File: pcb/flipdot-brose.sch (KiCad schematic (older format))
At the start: 5 parts, among them J1 Conn_02x30_Odd_Even, J2 Conn_01x03, U1 ESP32_DEVCITV1

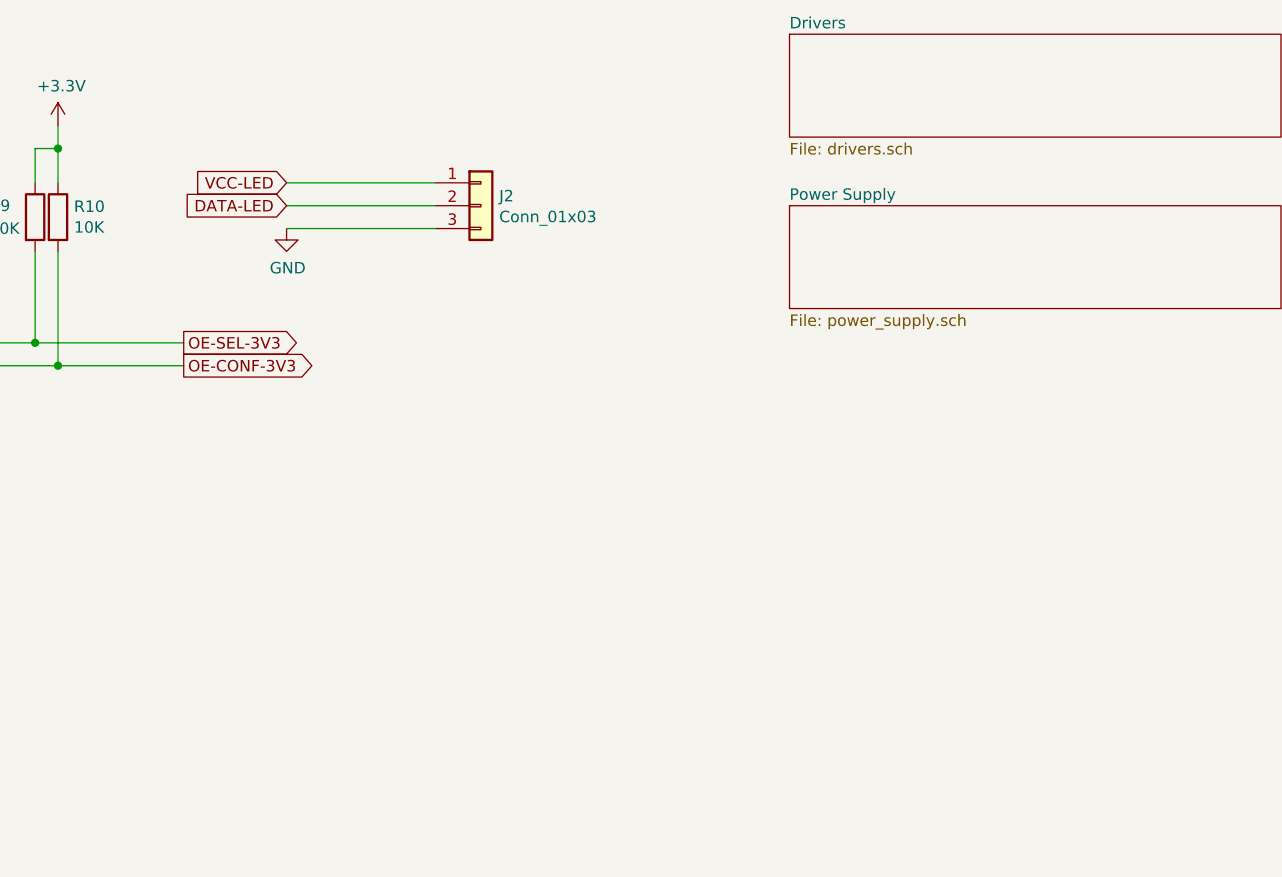
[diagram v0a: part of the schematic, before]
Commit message: resistor/capacitor for leds
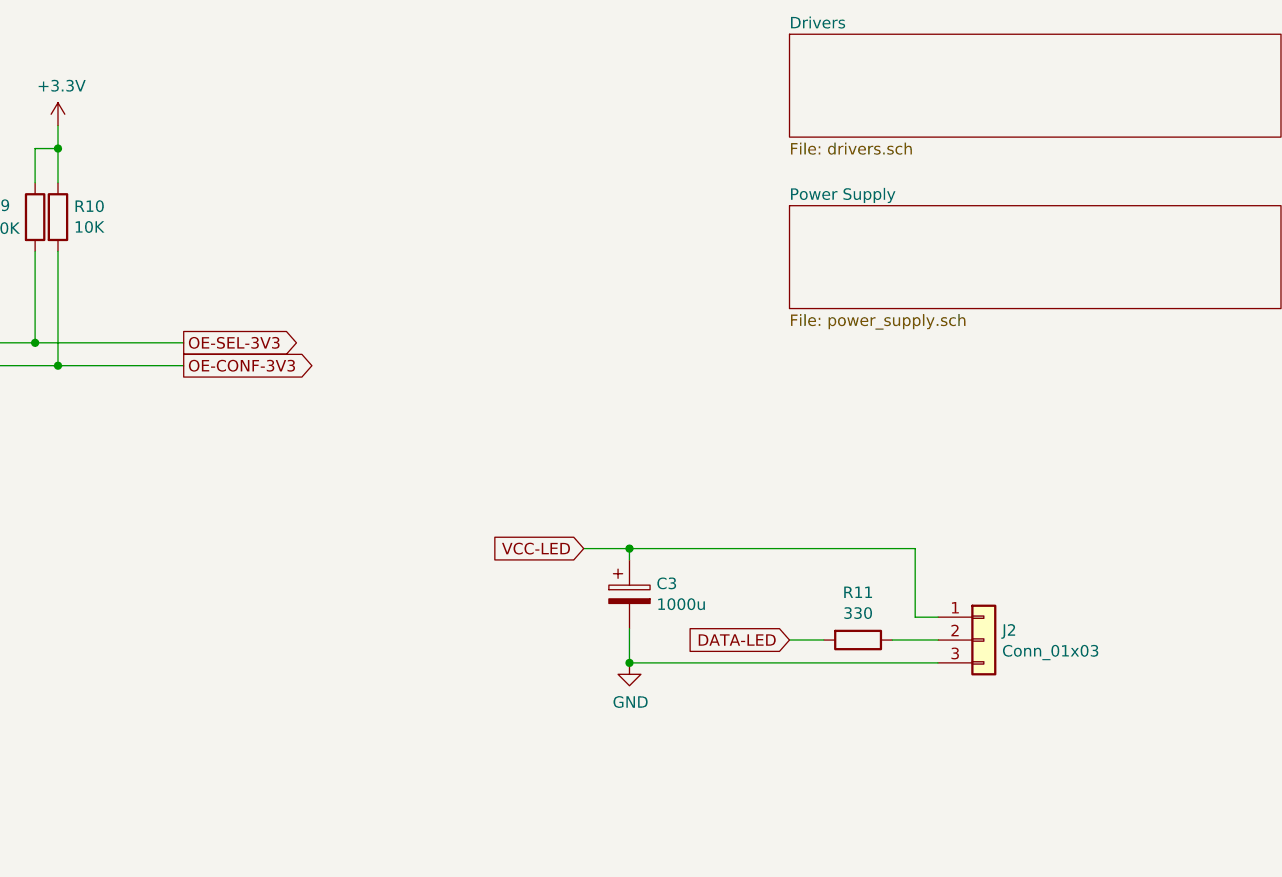
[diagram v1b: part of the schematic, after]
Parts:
- added C3: 1000u, Capacitor_THT:CP_Radial_D10.0mm_P5.00mm, symbol Device:CP
- added R11: 330, Resistor_THT:R_Axial_DIN0204_L3.6mm_D1.6mm_P5.08mm_Horizontal, symbol Device:R
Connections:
- net DATA-LED: now also R11.2; no longer J2.2 (Pin_2)
- net GND: now also C3.2
- net VCC-LED: now also C3.1
- new net: J2.2 (Pin_2), R11.1
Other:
- moved on the sheet: J2
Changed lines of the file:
@@
 	4400 2600 4600 2600
 Wire Wire Line
-	7250 1500 6600 1500
-Wire Wire Line
-	7250 1600 6600 1600
+	9450 3400 9250 3400
 $Comp
 L power:GND #PWR0102
 U 1 1 5DDF6886
-P 6600 1600
-F 0 "#PWR0102" H 6600 1350 50  0001 C CNN
-F 1 "GND" H 6605 1427 50  0000 C CNN
-F 2 "" H 6600 1600 50  0001 C CNN
-F 3 "" H 6600 1600 50  0001 C CNN
-	1    6600 1600
-	1    0    0    -1
-$EndComp
-Text GLabel 6600 1400 0    50   Input ~ 0
+P 8100 3500
+F 0 "#PWR0102" H 8100 3250 50  0001 C CNN
+F 1 "GND" H 8105 3327 50  0000 C CNN
+F 2 "" H 8100 3500 50  0001 C CNN
+F 3 "" H 8100 3500 50  0001 C CNN
+	1    8100 3500
+	1    0    0    -1
+$EndComp
+Text GLabel 7900 3000 0    50   Input ~ 0
 VCC-LED
-Text GLabel 6600 1500 0    50   Input ~ 0
+Text GLabel 8800 3400 0    50   Input ~ 0
 DATA-LED
 Wire Wire Line
@@
 L Connector_Generic:Conn_01x03 J2
 U 1 1 5DEADF32
-P 7450 1500
-F 0 "J2" H 7530 1542 50  0000 L CNN
-F 1 "Conn_01x03" H 7530 1451 50  0000 L CNN
-F 2 "Connectors_JST:JST_VH_B3PS-VH_2x3x3.96mm_Horizontal" H 7450 1500 50  0001 C CNN
-F 3 "~" H 7450 1500 50  0001 C CNN
-	1    7450 1500
-	1    0    0    -1
-$EndComp
-Wire Wire Line
-	6600 1400 7250 1400
+P 9650 3400
+F 0 "J2" H 9730 3442 50  0000 L CNN
+F 1 "Conn_01x03" H 9730 3351 50  0000 L CNN
+F 2 "Connectors_JST:JST_VH_B3PS-VH_2x3x3.96mm_Horizontal" H 9650 3400 50  0001 C CNN
+F 3 "~" H 9650 3400 50  0001 C CNN
+	1    9650 3400
+	1    0    0    -1
+$EndComp
 Wire Wire Line
 	5500 2100 6150 2100
@@
 	4400 1700 4600 1700
 NoConn ~ 4400 2100
+$Comp
+L Device:R R11
+U 1 1 5E7E658D
+P 9100 3400
+F 0 "R11" V 8893 3400 50  0000 C CNN
+F 1 "330" V 8984 3400 50  0000 C CNN
+F 2 "Resistor_THT:R_Axial_DIN0204_L3.6mm_D1.6mm_P5.08mm_Horizontal" V 9030 3400 50  0001 C CNN
+F 3 "~" H 9100 3400 50  0001 C CNN
+	1    9100 3400
+	0    1    1    0
+$EndComp
+Wire Wire Line
+	8950 3400 8800 3400
+Wire Wire Line
+	9450 3300 9350 3300
+Wire Wire Line
+	9350 3300 9350 3000
+Wire Wire Line
+	8100 3500 9450 3500
+$Comp
+L Device:CP C3
+U 1 1 5E7FAC58
+P 8100 3200
+F 0 "C3" H 8218 3246 50  0000 L CNN
+F 1 "1000u" H 8218 3155 50  0000 L CNN
+F 2 "Capacitor_THT:CP_Radial_D10.0mm_P5.00mm" H 8138 3050 50  0001 C CNN
+F 3 "~" H 8100 3200 50  0001 C CNN
+	1    8100 3200
+	1    0    0    -1
+$EndComp
+Wire Wire Line
+	7900 3000 8100 3000
+Wire Wire Line
+	8100 3050 8100 3000
+Connection ~ 8100 3000
+Wire Wire Line
+	8100 3000 9350 3000
+Wire Wire Line
+	8100 3350 8100 3500
+Connection ~ 8100 3500
 $EndSCHEMATC
